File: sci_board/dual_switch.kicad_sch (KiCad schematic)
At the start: 7 parts, among them U11 MIC2009YM6-TR, U12 MIC2009YM6-TR, U13 MIC2009YM6-TR

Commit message: continue layout
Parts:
- renumbered R19 to R20, R20 to R21, R21 to R22, R22 to R23
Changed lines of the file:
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@@
 		(dnp no)
 		(fields_autoplaced yes)
-		(property "Reference" "R20"
+		(property "Reference" "R21"
 			(at 201.295 81.2799 0)
 			(effects
@@
 			(project "sci_board"
 				(path "/b4b2c88d-f6cd-4e60-862d-e21f68728580/5e5b27f8-7a4c-45d0-95f8-aff71797fcd3/09c52fbd-a66a-456f-a3b3-a583ddfe7084"
-					(reference "R20")
-					(unit 1)
-				)
-				(path "/b4b2c88d-f6cd-4e60-862d-e21f68728580/5e5b27f8-7a4c-45d0-95f8-aff71797fcd3/3113fc14-4b9f-4852-8ddb-4c564d791d7f"
-					(reference "R12")
-					(unit 1)
-				)
-				(path "/b4b2c88d-f6cd-4e60-862d-e21f68728580/5e5b27f8-7a4c-45d0-95f8-aff71797fcd3/df99859d-8e37-4f21-a1c5-637d9e74b907"
-					(reference "R16")
+					(reference "R21")
+					(unit 1)
+				)
+				(path "/b4b2c88d-f6cd-4e60-862d-e21f68728580/5e5b27f8-7a4c-45d0-95f8-aff71797fcd3/3113fc14-4b9f-4852-8ddb-4c564d791d7f"
+					(reference "R13")
+					(unit 1)
+				)
+				(path "/b4b2c88d-f6cd-4e60-862d-e21f68728580/5e5b27f8-7a4c-45d0-95f8-aff71797fcd3/df99859d-8e37-4f21-a1c5-637d9e74b907"
+					(reference "R17")
 					(unit 1)
 				)
@@
 		(dnp no)
 		(fields_autoplaced yes)
-		(property "Reference" "R19"
+		(property "Reference" "R20"
 			(at 114.3 67.3099 0)
 			(effects
@@
 			(project "sci_board"
 				(path "/b4b2c88d-f6cd-4e60-862d-e21f68728580/5e5b27f8-7a4c-45d0-95f8-aff71797fcd3/09c52fbd-a66a-456f-a3b3-a583ddfe7084"
-					(reference "R19")
-					(unit 1)
-				)
-				(path "/b4b2c88d-f6cd-4e60-862d-e21f68728580/5e5b27f8-7a4c-45d0-95f8-aff71797fcd3/3113fc14-4b9f-4852-8ddb-4c564d791d7f"
-					(reference "R11")
-					(unit 1)
-				)
-				(path "/b4b2c88d-f6cd-4e60-862d-e21f68728580/5e5b27f8-7a4c-45d0-95f8-aff71797fcd3/df99859d-8e37-4f21-a1c5-637d9e74b907"
-					(reference "R15")
+					(reference "R20")
+					(unit 1)
+				)
+				(path "/b4b2c88d-f6cd-4e60-862d-e21f68728580/5e5b27f8-7a4c-45d0-95f8-aff71797fcd3/3113fc14-4b9f-4852-8ddb-4c564d791d7f"
+					(reference "R12")
+					(unit 1)
+				)
+				(path "/b4b2c88d-f6cd-4e60-862d-e21f68728580/5e5b27f8-7a4c-45d0-95f8-aff71797fcd3/df99859d-8e37-4f21-a1c5-637d9e74b907"
+					(reference "R16")
 					(unit 1)
 				)
@@
 		(dnp no)
 		(fields_autoplaced yes)
-		(property "Reference" "R21"
+		(property "Reference" "R22"
 			(at 133.35 81.9149 0)
 			(effects
@@
 			(project "sci_board"
 				(path "/b4b2c88d-f6cd-4e60-862d-e21f68728580/5e5b27f8-7a4c-45d0-95f8-aff71797fcd3/09c52fbd-a66a-456f-a3b3-a583ddfe7084"
-					(reference "R21")
-					(unit 1)
-				)
-				(path "/b4b2c88d-f6cd-4e60-862d-e21f68728580/5e5b27f8-7a4c-45d0-95f8-aff71797fcd3/3113fc14-4b9f-4852-8ddb-4c564d791d7f"
-					(reference "R13")
-					(unit 1)
-				)
-				(path "/b4b2c88d-f6cd-4e60-862d-e21f68728580/5e5b27f8-7a4c-45d0-95f8-aff71797fcd3/df99859d-8e37-4f21-a1c5-637d9e74b907"
-					(reference "R17")
+					(reference "R22")
+					(unit 1)
+				)
+				(path "/b4b2c88d-f6cd-4e60-862d-e21f68728580/5e5b27f8-7a4c-45d0-95f8-aff71797fcd3/3113fc14-4b9f-4852-8ddb-4c564d791d7f"
+					(reference "R14")
+					(unit 1)
+				)
+				(path "/b4b2c88d-f6cd-4e60-862d-e21f68728580/5e5b27f8-7a4c-45d0-95f8-aff71797fcd3/df99859d-8e37-4f21-a1c5-637d9e74b907"
+					(reference "R18")
 					(unit 1)
 				)
@@
 		(dnp no)
 		(fields_autoplaced yes)
-		(property "Reference" "R22"
+		(property "Reference" "R23"
 			(at 61.595 82.5499 0)
 			(effects
@@
 			(project "sci_board"
 				(path "/b4b2c88d-f6cd-4e60-862d-e21f68728580/5e5b27f8-7a4c-45d0-95f8-aff71797fcd3/09c52fbd-a66a-456f-a3b3-a583ddfe7084"
-					(reference "R22")
-					(unit 1)
-				)
-				(path "/b4b2c88d-f6cd-4e60-862d-e21f68728580/5e5b27f8-7a4c-45d0-95f8-aff71797fcd3/3113fc14-4b9f-4852-8ddb-4c564d791d7f"
-					(reference "R14")
-					(unit 1)
-				)
-				(path "/b4b2c88d-f6cd-4e60-862d-e21f68728580/5e5b27f8-7a4c-45d0-95f8-aff71797fcd3/df99859d-8e37-4f21-a1c5-637d9e74b907"
-					(reference "R18")
-					(unit 1)
-				)
+					(reference "R23")
+					(unit 1)
+				)
+				(path "/b4b2c88d-f6cd-4e60-862d-e21f68728580/5e5b27f8-7a4c-45d0-95f8-aff71797fcd3/3113fc14-4b9f-4852-8ddb-4c564d791d7f"
+					(reference "R15")
+					(unit 1)
+				)
+				(path "/b4b2c88d-f6cd-4e60-862d-e21f68728580/5e5b27f8-7a4c-45d0-95f8-aff71797fcd3/df99859d-8e37-4f21-a1c5-637d9e74b907"
+					(reference "R19")
+					(unit 1)
+				)

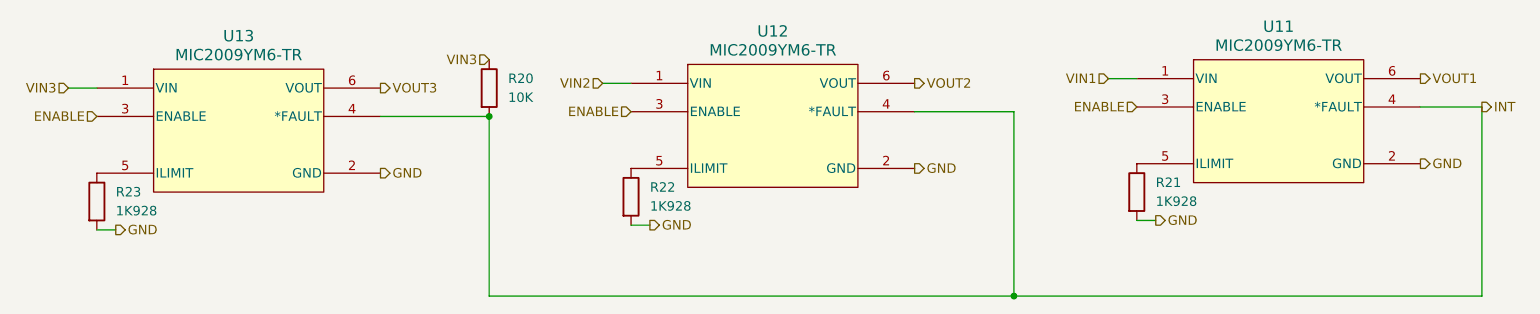
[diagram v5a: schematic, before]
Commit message: changed over SCI to smaller footprint switches
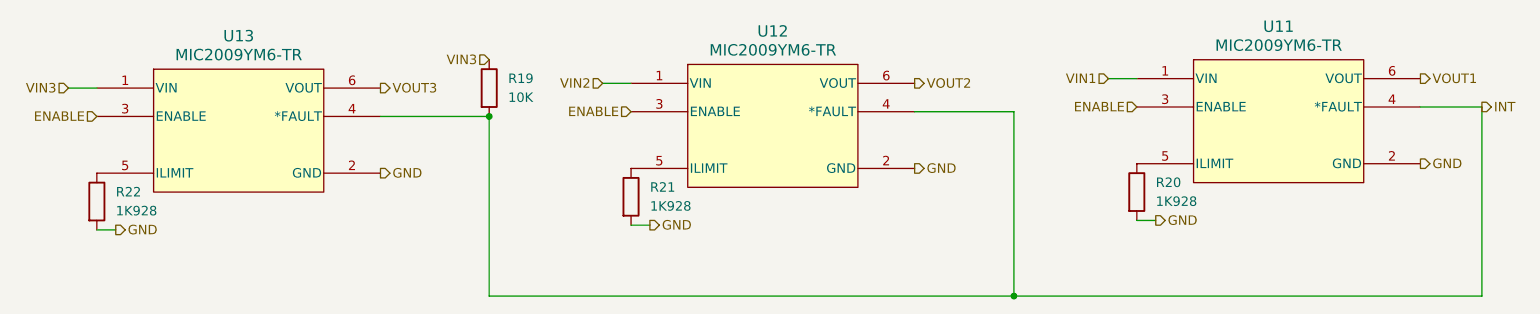
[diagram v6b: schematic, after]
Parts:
- R19: renamed from R20; footprint Resistor_SMD:R_0603_1608Metric_Pad0.98x0.95mm_HandSolder -> Resistor_SMD:R_0402_1005Metric_Pad0.72x0.64mm_HandSolder
- renumbered R21 to R20, R22 to R21, R23 to R22
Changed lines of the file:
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@@
 		(dnp no)
 		(fields_autoplaced yes)
-		(property "Reference" "R21"
+		(property "Reference" "R20"
 			(at 201.295 81.2799 0)
 			(effects
@@
 			(project "sci_board"
 				(path "/b4b2c88d-f6cd-4e60-862d-e21f68728580/5e5b27f8-7a4c-45d0-95f8-aff71797fcd3/09c52fbd-a66a-456f-a3b3-a583ddfe7084"
-					(reference "R21")
-					(unit 1)
-				)
-				(path "/b4b2c88d-f6cd-4e60-862d-e21f68728580/5e5b27f8-7a4c-45d0-95f8-aff71797fcd3/3113fc14-4b9f-4852-8ddb-4c564d791d7f"
-					(reference "R13")
-					(unit 1)
-				)
-				(path "/b4b2c88d-f6cd-4e60-862d-e21f68728580/5e5b27f8-7a4c-45d0-95f8-aff71797fcd3/df99859d-8e37-4f21-a1c5-637d9e74b907"
-					(reference "R17")
+					(reference "R20")
+					(unit 1)
+				)
+				(path "/b4b2c88d-f6cd-4e60-862d-e21f68728580/5e5b27f8-7a4c-45d0-95f8-aff71797fcd3/3113fc14-4b9f-4852-8ddb-4c564d791d7f"
+					(reference "R12")
+					(unit 1)
+				)
+				(path "/b4b2c88d-f6cd-4e60-862d-e21f68728580/5e5b27f8-7a4c-45d0-95f8-aff71797fcd3/df99859d-8e37-4f21-a1c5-637d9e74b907"
+					(reference "R16")
 					(unit 1)
 				)
@@
 		(dnp no)
 		(fields_autoplaced yes)
-		(property "Reference" "R20"
+		(property "Reference" "R19"
 			(at 114.3 67.3099 0)
 			(effects
@@
 			)
 		)
-		(property "Footprint" "Resistor_SMD:R_0603_1608Metric_Pad0.98x0.95mm_HandSolder"
+		(property "Footprint" "Resistor_SMD:R_0402_1005Metric_Pad0.72x0.64mm_HandSolder"
 			(at 109.982 68.58 90)
 			(effects
@@
 			(project "sci_board"
 				(path "/b4b2c88d-f6cd-4e60-862d-e21f68728580/5e5b27f8-7a4c-45d0-95f8-aff71797fcd3/09c52fbd-a66a-456f-a3b3-a583ddfe7084"
-					(reference "R20")
-					(unit 1)
-				)
-				(path "/b4b2c88d-f6cd-4e60-862d-e21f68728580/5e5b27f8-7a4c-45d0-95f8-aff71797fcd3/3113fc14-4b9f-4852-8ddb-4c564d791d7f"
-					(reference "R12")
-					(unit 1)
-				)
-				(path "/b4b2c88d-f6cd-4e60-862d-e21f68728580/5e5b27f8-7a4c-45d0-95f8-aff71797fcd3/df99859d-8e37-4f21-a1c5-637d9e74b907"
-					(reference "R16")
+					(reference "R19")
+					(unit 1)
+				)
+				(path "/b4b2c88d-f6cd-4e60-862d-e21f68728580/5e5b27f8-7a4c-45d0-95f8-aff71797fcd3/3113fc14-4b9f-4852-8ddb-4c564d791d7f"
+					(reference "R11")
+					(unit 1)
+				)
+				(path "/b4b2c88d-f6cd-4e60-862d-e21f68728580/5e5b27f8-7a4c-45d0-95f8-aff71797fcd3/df99859d-8e37-4f21-a1c5-637d9e74b907"
+					(reference "R15")
 					(unit 1)
 				)
@@
 		(dnp no)
 		(fields_autoplaced yes)
-		(property "Reference" "R22"
+		(property "Reference" "R21"
 			(at 133.35 81.9149 0)
 			(effects
@@
 			(project "sci_board"
 				(path "/b4b2c88d-f6cd-4e60-862d-e21f68728580/5e5b27f8-7a4c-45d0-95f8-aff71797fcd3/09c52fbd-a66a-456f-a3b3-a583ddfe7084"
-					(reference "R22")
-					(unit 1)
-				)
-				(path "/b4b2c88d-f6cd-4e60-862d-e21f68728580/5e5b27f8-7a4c-45d0-95f8-aff71797fcd3/3113fc14-4b9f-4852-8ddb-4c564d791d7f"
-					(reference "R14")
-					(unit 1)
-				)
-				(path "/b4b2c88d-f6cd-4e60-862d-e21f68728580/5e5b27f8-7a4c-45d0-95f8-aff71797fcd3/df99859d-8e37-4f21-a1c5-637d9e74b907"
-					(reference "R18")
+					(reference "R21")
+					(unit 1)
+				)
+				(path "/b4b2c88d-f6cd-4e60-862d-e21f68728580/5e5b27f8-7a4c-45d0-95f8-aff71797fcd3/3113fc14-4b9f-4852-8ddb-4c564d791d7f"
+					(reference "R13")
+					(unit 1)
+				)
+				(path "/b4b2c88d-f6cd-4e60-862d-e21f68728580/5e5b27f8-7a4c-45d0-95f8-aff71797fcd3/df99859d-8e37-4f21-a1c5-637d9e74b907"
+					(reference "R17")
 					(unit 1)
 				)
@@
 		(dnp no)
 		(fields_autoplaced yes)
-		(property "Reference" "R23"
+		(property "Reference" "R22"
 			(at 61.595 82.5499 0)
 			(effects
@@
 			(project "sci_board"
 				(path "/b4b2c88d-f6cd-4e60-862d-e21f68728580/5e5b27f8-7a4c-45d0-95f8-aff71797fcd3/09c52fbd-a66a-456f-a3b3-a583ddfe7084"
-					(reference "R23")
-					(unit 1)
-				)
-				(path "/b4b2c88d-f6cd-4e60-862d-e21f68728580/5e5b27f8-7a4c-45d0-95f8-aff71797fcd3/3113fc14-4b9f-4852-8ddb-4c564d791d7f"
-					(reference "R15")
-					(unit 1)
-				)
-				(path "/b4b2c88d-f6cd-4e60-862d-e21f68728580/5e5b27f8-7a4c-45d0-95f8-aff71797fcd3/df99859d-8e37-4f21-a1c5-637d9e74b907"
-					(reference "R19")
-					(unit 1)
-				)
+					(reference "R22")
+					(unit 1)
+				)
+				(path "/b4b2c88d-f6cd-4e60-862d-e21f68728580/5e5b27f8-7a4c-45d0-95f8-aff71797fcd3/3113fc14-4b9f-4852-8ddb-4c564d791d7f"
+					(reference "R14")
+					(unit 1)
+				)
+				(path "/b4b2c88d-f6cd-4e60-862d-e21f68728580/5e5b27f8-7a4c-45d0-95f8-aff71797fcd3/df99859d-8e37-4f21-a1c5-637d9e74b907"
+					(reference "R18")
+					(unit 1)
+				)

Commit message: replace nearly all buck converters with boost buck (missing is 5raw
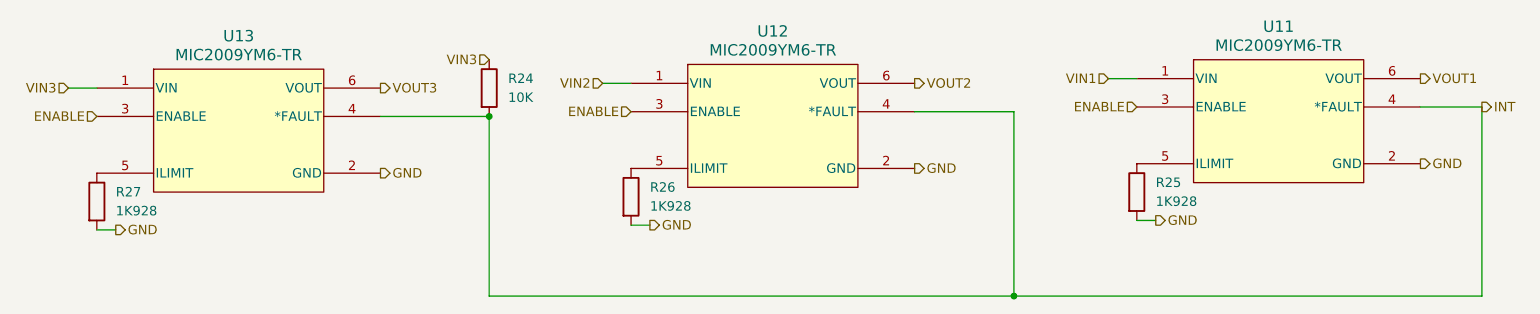
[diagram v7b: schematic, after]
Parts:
- renumbered R19 to R24, R20 to R25, R21 to R26, R22 to R27
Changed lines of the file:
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@@
 		(dnp no)
 		(fields_autoplaced yes)
-		(property "Reference" "R20"
+		(property "Reference" "R25"
 			(at 201.295 81.2799 0)
 			(effects
@@
 			(project "sci_board"
 				(path "/b4b2c88d-f6cd-4e60-862d-e21f68728580/5e5b27f8-7a4c-45d0-95f8-aff71797fcd3/09c52fbd-a66a-456f-a3b3-a583ddfe7084"
-					(reference "R20")
-					(unit 1)
-				)
-				(path "/b4b2c88d-f6cd-4e60-862d-e21f68728580/5e5b27f8-7a4c-45d0-95f8-aff71797fcd3/3113fc14-4b9f-4852-8ddb-4c564d791d7f"
-					(reference "R12")
-					(unit 1)
-				)
-				(path "/b4b2c88d-f6cd-4e60-862d-e21f68728580/5e5b27f8-7a4c-45d0-95f8-aff71797fcd3/df99859d-8e37-4f21-a1c5-637d9e74b907"
-					(reference "R16")
+					(reference "R25")
+					(unit 1)
+				)
+				(path "/b4b2c88d-f6cd-4e60-862d-e21f68728580/5e5b27f8-7a4c-45d0-95f8-aff71797fcd3/3113fc14-4b9f-4852-8ddb-4c564d791d7f"
+					(reference "R17")
+					(unit 1)
+				)
+				(path "/b4b2c88d-f6cd-4e60-862d-e21f68728580/5e5b27f8-7a4c-45d0-95f8-aff71797fcd3/df99859d-8e37-4f21-a1c5-637d9e74b907"
+					(reference "R21")
 					(unit 1)
 				)
@@
 		(dnp no)
 		(fields_autoplaced yes)
-		(property "Reference" "R19"
+		(property "Reference" "R24"
 			(at 114.3 67.3099 0)
 			(effects
@@
 			(project "sci_board"
 				(path "/b4b2c88d-f6cd-4e60-862d-e21f68728580/5e5b27f8-7a4c-45d0-95f8-aff71797fcd3/09c52fbd-a66a-456f-a3b3-a583ddfe7084"
-					(reference "R19")
-					(unit 1)
-				)
-				(path "/b4b2c88d-f6cd-4e60-862d-e21f68728580/5e5b27f8-7a4c-45d0-95f8-aff71797fcd3/3113fc14-4b9f-4852-8ddb-4c564d791d7f"
-					(reference "R11")
-					(unit 1)
-				)
-				(path "/b4b2c88d-f6cd-4e60-862d-e21f68728580/5e5b27f8-7a4c-45d0-95f8-aff71797fcd3/df99859d-8e37-4f21-a1c5-637d9e74b907"
-					(reference "R15")
+					(reference "R24")
+					(unit 1)
+				)
+				(path "/b4b2c88d-f6cd-4e60-862d-e21f68728580/5e5b27f8-7a4c-45d0-95f8-aff71797fcd3/3113fc14-4b9f-4852-8ddb-4c564d791d7f"
+					(reference "R16")
+					(unit 1)
+				)
+				(path "/b4b2c88d-f6cd-4e60-862d-e21f68728580/5e5b27f8-7a4c-45d0-95f8-aff71797fcd3/df99859d-8e37-4f21-a1c5-637d9e74b907"
+					(reference "R20")
 					(unit 1)
 				)
@@
 		(dnp no)
 		(fields_autoplaced yes)
-		(property "Reference" "R21"
+		(property "Reference" "R26"
 			(at 133.35 81.9149 0)
 			(effects
@@
 			(project "sci_board"
 				(path "/b4b2c88d-f6cd-4e60-862d-e21f68728580/5e5b27f8-7a4c-45d0-95f8-aff71797fcd3/09c52fbd-a66a-456f-a3b3-a583ddfe7084"
-					(reference "R21")
-					(unit 1)
-				)
-				(path "/b4b2c88d-f6cd-4e60-862d-e21f68728580/5e5b27f8-7a4c-45d0-95f8-aff71797fcd3/3113fc14-4b9f-4852-8ddb-4c564d791d7f"
-					(reference "R13")
-					(unit 1)
-				)
-				(path "/b4b2c88d-f6cd-4e60-862d-e21f68728580/5e5b27f8-7a4c-45d0-95f8-aff71797fcd3/df99859d-8e37-4f21-a1c5-637d9e74b907"
-					(reference "R17")
+					(reference "R26")
+					(unit 1)
+				)
+				(path "/b4b2c88d-f6cd-4e60-862d-e21f68728580/5e5b27f8-7a4c-45d0-95f8-aff71797fcd3/3113fc14-4b9f-4852-8ddb-4c564d791d7f"
+					(reference "R18")
+					(unit 1)
+				)
+				(path "/b4b2c88d-f6cd-4e60-862d-e21f68728580/5e5b27f8-7a4c-45d0-95f8-aff71797fcd3/df99859d-8e37-4f21-a1c5-637d9e74b907"
+					(reference "R22")
 					(unit 1)
 				)
@@
 		(dnp no)
 		(fields_autoplaced yes)
-		(property "Reference" "R22"
+		(property "Reference" "R27"
 			(at 61.595 82.5499 0)
 			(effects
@@
 			(project "sci_board"
 				(path "/b4b2c88d-f6cd-4e60-862d-e21f68728580/5e5b27f8-7a4c-45d0-95f8-aff71797fcd3/09c52fbd-a66a-456f-a3b3-a583ddfe7084"
-					(reference "R22")
-					(unit 1)
-				)
-				(path "/b4b2c88d-f6cd-4e60-862d-e21f68728580/5e5b27f8-7a4c-45d0-95f8-aff71797fcd3/3113fc14-4b9f-4852-8ddb-4c564d791d7f"
-					(reference "R14")
-					(unit 1)
-				)
-				(path "/b4b2c88d-f6cd-4e60-862d-e21f68728580/5e5b27f8-7a4c-45d0-95f8-aff71797fcd3/df99859d-8e37-4f21-a1c5-637d9e74b907"
-					(reference "R18")
-					(unit 1)
-				)
+					(reference "R27")
+					(unit 1)
+				)
+				(path "/b4b2c88d-f6cd-4e60-862d-e21f68728580/5e5b27f8-7a4c-45d0-95f8-aff71797fcd3/3113fc14-4b9f-4852-8ddb-4c564d791d7f"
+					(reference "R19")
+					(unit 1)
+				)
+				(path "/b4b2c88d-f6cd-4e60-862d-e21f68728580/5e5b27f8-7a4c-45d0-95f8-aff71797fcd3/df99859d-8e37-4f21-a1c5-637d9e74b907"
+					(reference "R23")
+					(unit 1)
+				)

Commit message: SCI BOM updated
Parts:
- R24: Manufacturer (none) -> YAGEO; Note (none) -> INT pullup; Part Number (none) -> RC0402FR-0710KL; Tolerance (none) -> 1
- R25, R26, R27: value 1K928 -> 1K5; Manufacturer (none) -> YAGEO; Note (none) -> Current limited; Part Number (none) -> RC0603FR-071K5L; Tolerance (none) -> 1
- U10: renamed from U11; Manufacturer (none) -> Microchip Technology; Part Number (none) -> MIC2009YM6-TR
- U11: renamed from U12; Manufacturer (none) -> Microchip Technology; Part Number (none) -> MIC2009YM6-TR
- U12: renamed from U13; Manufacturer (none) -> Microchip Technology; Part Number (none) -> MIC2009YM6-TR
